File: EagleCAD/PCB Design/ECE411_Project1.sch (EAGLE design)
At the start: 25 parts, among them J1 0473460001_USBMICRO, SW1 FSM2JSMLTR, U1 ATS160SM-1, U2 MIC29310-5.0WU, U3 NCP5501DT50RKG

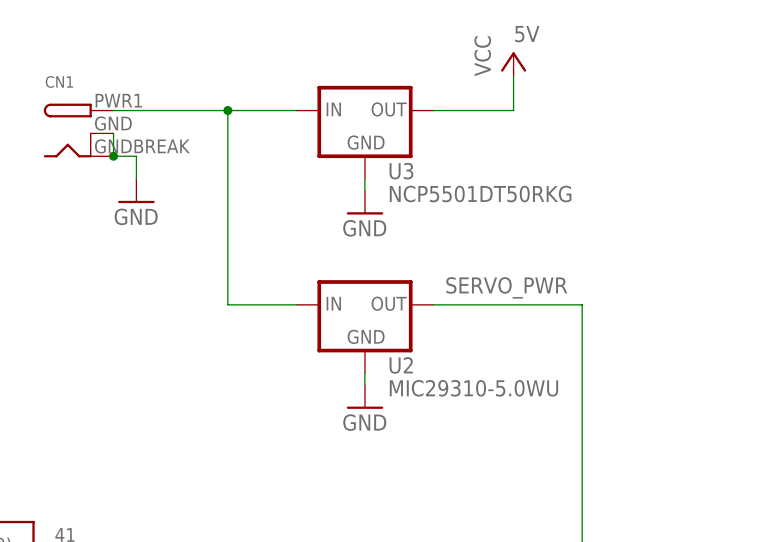
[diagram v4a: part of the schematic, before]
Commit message: Visually complete schematic - nets need to be named still, and erc needs to be run.
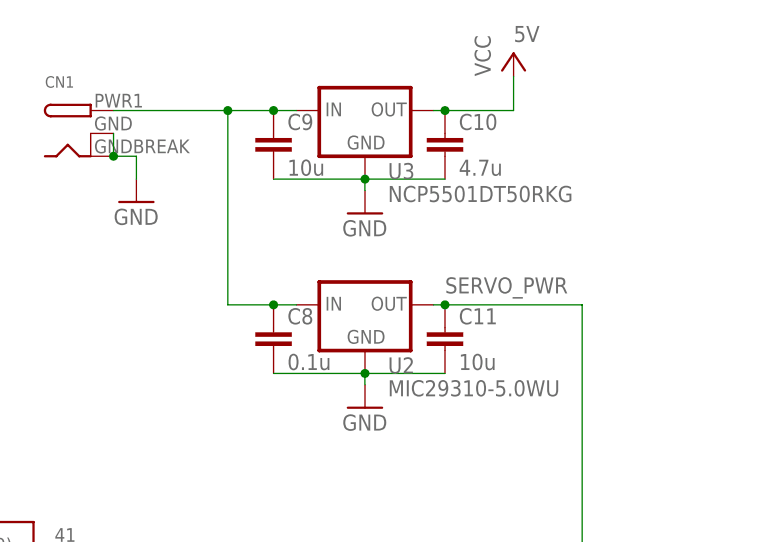
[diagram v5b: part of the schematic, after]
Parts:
- added C10: 4.7u, rcl:C-EUC1206
- added C11, C9: 10u, rcl:C-EUC1206
- added C8: 0.1u, rcl:C-EUC1206
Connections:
- net GND: now also C10.2, C11.2, C8.2, C9.2
- net N$22: now also C8.1, C9.1
- net SERVO_PWR: now also C11.1
- net VCC: now also C10.1
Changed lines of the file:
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@@
 </part>
 <part name="GND15" library="supply1" library_urn="urn:adsk.eagle:library:371" deviceset="GND" device=""/>
+<part name="C8" library="rcl" library_urn="urn:adsk.eagle:library:334" deviceset="C-EU" device="C1206" package3d_urn="urn:adsk.eagle:package:23618/2" value="0.1u"/>
+<part name="C9" library="rcl" library_urn="urn:adsk.eagle:library:334" deviceset="C-EU" device="C1206" package3d_urn="urn:adsk.eagle:package:23618/2" value="10u"/>
+<part name="C10" library="rcl" library_urn="urn:adsk.eagle:library:334" deviceset="C-EU" device="C1206" package3d_urn="urn:adsk.eagle:package:23618/2" value="4.7u"/>
+<part name="C11" library="rcl" library_urn="urn:adsk.eagle:library:334" deviceset="C-EU" device="C1206" package3d_urn="urn:adsk.eagle:package:23618/2" value="10u"/>
 </parts>
 <sheets>
@@
 </instance>
 <instance part="GND15" gate="1" x="33.02" y="121.92"/>
+<instance part="C8" gate="G$1" x="48.26" y="107.95"/>
+<instance part="C9" gate="G$1" x="48.26" y="129.54"/>
+<instance part="C10" gate="G$1" x="67.31" y="129.54"/>
+<instance part="C11" gate="G$1" x="67.31" y="107.95"/>
 </instances>
 <busses>
@@
 <wire x1="58.42" y1="102.87" x2="58.42" y2="101.6" width="0.1524" layer="91"/>
 <pinref part="GND9" gate="1" pin="GND"/>
+<pinref part="C8" gate="G$1" pin="2"/>
+<wire x1="48.26" y1="102.87" x2="58.42" y2="102.87" width="0.1524" layer="91"/>
+<junction x="58.42" y="102.87"/>
+<pinref part="C11" gate="G$1" pin="2"/>
+<wire x1="58.42" y1="102.87" x2="67.31" y2="102.87" width="0.1524" layer="91"/>
 </segment>
 <segment>
@@
 <wire x1="58.42" y1="124.46" x2="58.42" y2="123.19" width="0.1524" layer="91"/>
 <pinref part="GND10" gate="1" pin="GND"/>
+<pinref part="C9" gate="G$1" pin="2"/>
+<wire x1="48.26" y1="124.46" x2="58.42" y2="124.46" width="0.1524" layer="91"/>
+<junction x="58.42" y="124.46"/>
+<pinref part="C10" gate="G$1" pin="2"/>
+<wire x1="58.42" y1="124.46" x2="67.31" y2="124.46" width="0.1524" layer="91"/>
 </segment>
 <segment>
@@
 <segment>
 <pinref part="U3" gate="G$1" pin="OUT"/>
-<wire x1="66.04" y1="132.08" x2="74.93" y2="132.08" width="0.1524" layer="91"/>
+<wire x1="66.04" y1="132.08" x2="67.31" y2="132.08" width="0.1524" layer="91"/>
+<wire x1="67.31" y1="132.08" x2="74.93" y2="132.08" width="0.1524" layer="91"/>
 <wire x1="74.93" y1="132.08" x2="74.93" y2="135.89" width="0.1524" layer="91"/>
 <pinref part="P+4" gate="VCC" pin="VCC"/>
+<pinref part="C10" gate="G$1" pin="1"/>
+<junction x="67.31" y="132.08"/>
 </segment>
 </net>
@@
 <junction x="71.12" y="58.42"/>
 <pinref part="U2" gate="G$1" pin="OUT"/>
-<wire x1="82.55" y1="110.49" x2="66.04" y2="110.49" width="0.1524" layer="91"/>
+<wire x1="82.55" y1="110.49" x2="67.31" y2="110.49" width="0.1524" layer="91"/>
 <label x="67.31" y="111.76" size="1.778" layer="95"/>
+<pinref part="C11" gate="G$1" pin="1"/>
+<wire x1="67.31" y1="110.49" x2="66.04" y2="110.49" width="0.1524" layer="91"/>
+<junction x="67.31" y="110.49"/>
 </segment>
 </net>
@@
 <wire x1="30.48" y1="132.08" x2="43.18" y2="132.08" width="0.1524" layer="91"/>
 <pinref part="U2" gate="G$1" pin="IN"/>
-<wire x1="43.18" y1="132.08" x2="50.8" y2="132.08" width="0.1524" layer="91"/>
-<wire x1="50.8" y1="110.49" x2="43.18" y2="110.49" width="0.1524" layer="91"/>
+<wire x1="43.18" y1="132.08" x2="48.26" y2="132.08" width="0.1524" layer="91"/>
+<wire x1="48.26" y1="132.08" x2="50.8" y2="132.08" width="0.1524" layer="91"/>
+<wire x1="50.8" y1="110.49" x2="48.26" y2="110.49" width="0.1524" layer="91"/>
+<wire x1="48.26" y1="110.49" x2="43.18" y2="110.49" width="0.1524" layer="91"/>
 <wire x1="43.18" y1="110.49" x2="43.18" y2="132.08" width="0.1524" layer="91"/>
 <junction x="43.18" y="132.08"/>
-</segment>
-</net>
+<pinref part="C8" gate="G$1" pin="1"/>
+<junction x="48.26" y="110.49"/>
+<pinref part="C9" gate="G$1" pin="1"/>
+<junction x="48.26" y="132.08"/>
+</segment>
+</net>

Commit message: changed xtal caps to 0805 size from 1206
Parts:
- C6, C7: device rcl:C-EUC1206 -> rcl:C-EUC0805
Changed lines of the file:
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@@
 <part name="LED2" library="led" library_urn="urn:adsk.eagle:library:259" deviceset="LED" device="SMT1206" package3d_urn="urn:adsk.eagle:package:15796/1"/>
 <part name="LED1" library="led" library_urn="urn:adsk.eagle:library:259" deviceset="LED" device="SMT1206" package3d_urn="urn:adsk.eagle:package:15796/1"/>
-<part name="C6" library="rcl" library_urn="urn:adsk.eagle:library:334" deviceset="C-EU" device="C1206" package3d_urn="urn:adsk.eagle:package:23618/2" value="22p"/>
-<part name="C7" library="rcl" library_urn="urn:adsk.eagle:library:334" deviceset="C-EU" device="C1206" package3d_urn="urn:adsk.eagle:package:23618/2" value="22p"/>
 <part name="GND14" library="supply1" library_urn="urn:adsk.eagle:library:371" deviceset="GND" device=""/>
 <part name="P+2" library="supply1" library_urn="urn:adsk.eagle:library:371" deviceset="VCC" device="">
@@
 <part name="C10" library="rcl" library_urn="urn:adsk.eagle:library:334" deviceset="C-EU" device="C1206" package3d_urn="urn:adsk.eagle:package:23618/2" value="4.7u"/>
 <part name="C11" library="rcl" library_urn="urn:adsk.eagle:library:334" deviceset="C-EU" device="C1206" package3d_urn="urn:adsk.eagle:package:23618/2" value="10u"/>
+<part name="C6" library="rcl" library_urn="urn:adsk.eagle:library:334" deviceset="C-EU" device="C0805" package3d_urn="urn:adsk.eagle:package:23617/2" value="22p"/>
+<part name="C7" library="rcl" library_urn="urn:adsk.eagle:library:334" deviceset="C-EU" device="C0805" package3d_urn="urn:adsk.eagle:package:23617/2" value="22p"/>
 </parts>
 <sheets>
@@
 <instance part="LED2" gate="G$1" x="30.48" y="-10.16"/>
 <instance part="LED1" gate="G$1" x="39.37" y="-10.16"/>
-<instance part="C6" gate="G$1" x="-35.56" y="39.37" rot="R90"/>
-<instance part="C7" gate="G$1" x="-35.56" y="29.21" rot="R90"/>
 <instance part="GND14" gate="1" x="-38.1" y="24.13"/>
 <instance part="P+2" gate="VCC" x="-26.67" y="74.93">
@@
 <instance part="C10" gate="G$1" x="67.31" y="129.54"/>
 <instance part="C11" gate="G$1" x="67.31" y="107.95"/>
+<instance part="C6" gate="G$1" x="-35.56" y="39.37" rot="R90"/>
+<instance part="C7" gate="G$1" x="-35.56" y="29.21" rot="R90"/>
 </instances>
 <busses>
@@
 </segment>
 <segment>
+<wire x1="-38.1" y1="39.37" x2="-38.1" y2="29.21" width="0.1524" layer="91"/>
+<wire x1="-38.1" y1="29.21" x2="-38.1" y2="26.67" width="0.1524" layer="91"/>
+<pinref part="GND14" gate="1" pin="GND"/>
 <pinref part="C6" gate="G$1" pin="1"/>
 <pinref part="C7" gate="G$1" pin="1"/>
-<wire x1="-38.1" y1="39.37" x2="-38.1" y2="29.21" width="0.1524" layer="91"/>
-<wire x1="-38.1" y1="29.21" x2="-38.1" y2="26.67" width="0.1524" layer="91"/>
 <junction x="-38.1" y="29.21"/>
-<pinref part="GND14" gate="1" pin="GND"/>
 </segment>
 <segment>
@@
 <segment>
 <wire x1="-29.21" y1="29.21" x2="-26.67" y2="29.21" width="0.1524" layer="91"/>
-<pinref part="C7" gate="G$1" pin="2"/>
 <wire x1="-26.67" y1="29.21" x2="-24.13" y2="29.21" width="0.1524" layer="91"/>
 <wire x1="-29.21" y1="29.21" x2="-30.48" y2="29.21" width="0.1524" layer="91"/>
@@
 <pinref part="U1" gate="G$1" pin="1"/>
 <junction x="-26.67" y="29.21"/>
+<pinref part="C7" gate="G$1" pin="2"/>
 </segment>
 </net>
@@
 <segment>
 <wire x1="-24.13" y1="39.37" x2="-26.67" y2="39.37" width="0.1524" layer="91"/>
-<pinref part="C6" gate="G$1" pin="2"/>
 <wire x1="-26.67" y1="39.37" x2="-29.21" y2="39.37" width="0.1524" layer="91"/>
 <wire x1="-29.21" y1="39.37" x2="-30.48" y2="39.37" width="0.1524" layer="91"/>
@@
 <pinref part="U1" gate="G$1" pin="2"/>
 <junction x="-26.67" y="39.37"/>
-</segment>
-</net>
+<pinref part="C6" gate="G$1" pin="2"/>
+</segment>
+</net>

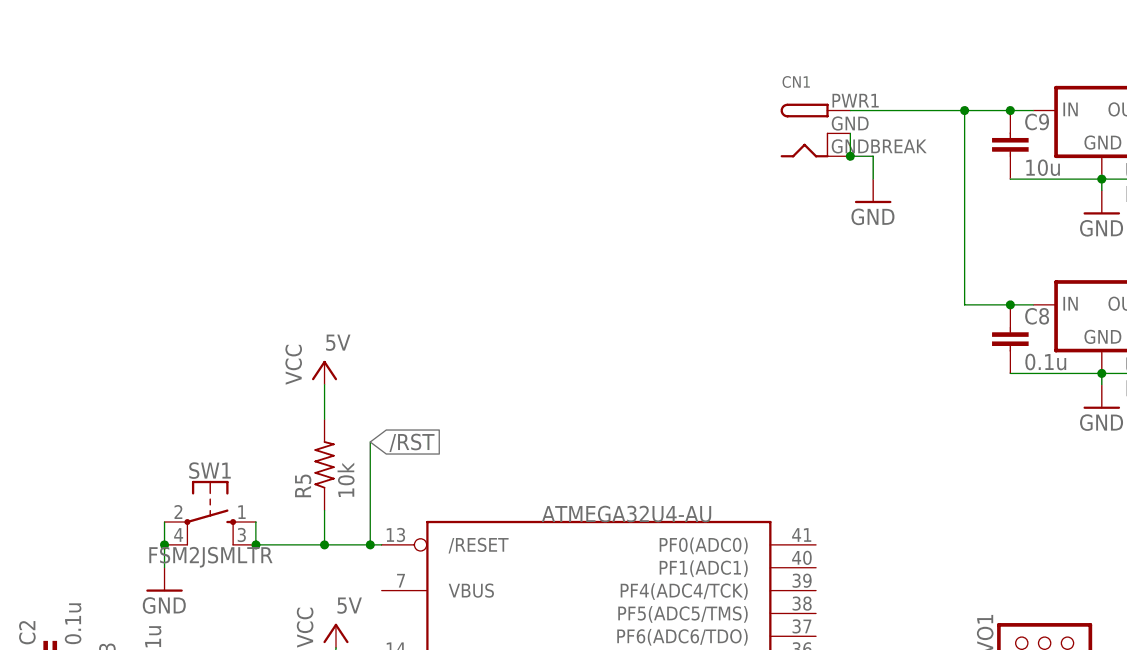
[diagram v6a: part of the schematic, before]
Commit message: Updated schematic with new DC barrel component that is thru-hole 2.1MM size
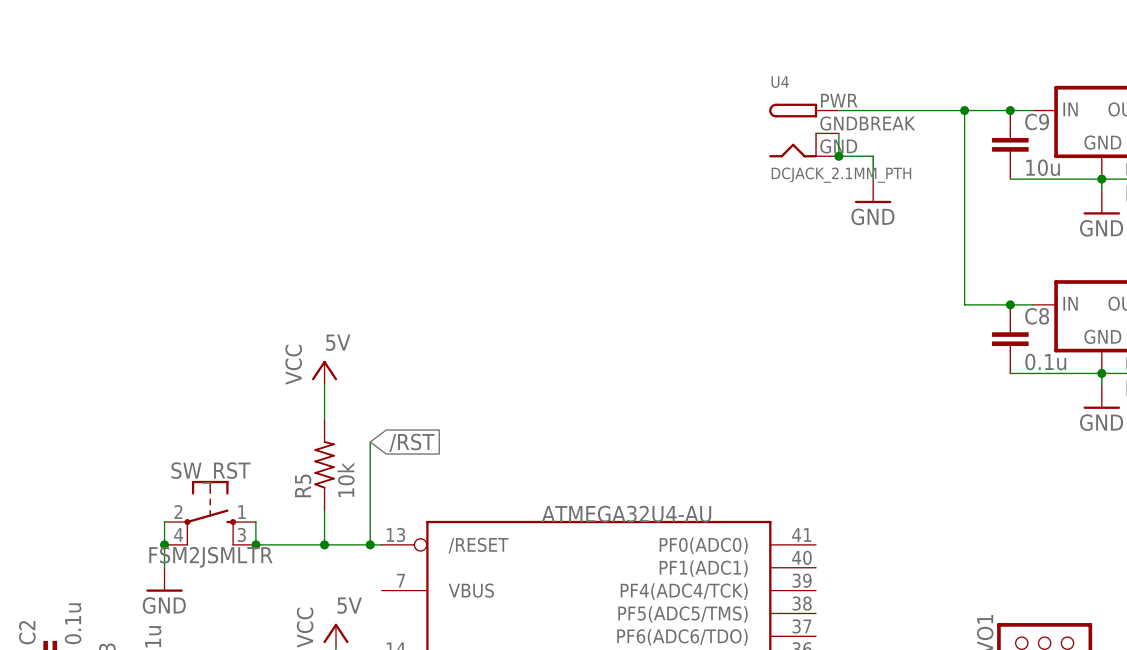
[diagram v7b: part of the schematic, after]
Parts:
- removed CN1: (no value), adafruit:DCBARRELSMT
- added U4: DCJACK_2.1MM_PTH, DCBARREL_2.1MM:DCJACK_2.1MM_PTH
- renumbered SW1 to SW_RST
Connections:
- net N$1 renamed D+USB
- net N$2 renamed D+MCU
- net N$3 renamed D-USB
- net N$4 renamed D-MCU
- net GND: now also U4.GND, U4.GNDBREAK; no longer CN1.GND, CN1.GNDBREAK
- net N$22: now also U4.PWR; no longer CN1.PWR
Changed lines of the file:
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@@
 <attribute name="VCC" value="5V"/>
 </part>
-<part name="SW1" library="Push_Button" deviceset="FSM2JSMLTR" device=""/>
+<part name="SW_RST" library="Push_Button" deviceset="FSM2JSMLTR" device=""/>
 <part name="J1" library="USB_Micro_and_AVRISP" deviceset="0473460001_USBMICRO" device=""/>
 <part name="ISP1" library="USB_Micro_and_AVRISP" deviceset="AVRISP" device="-6"/>
 <part name="U1" library="Xtals" deviceset="ATS160SM-1" device=""/>
-<part name="CN1" library="adafruit" library_urn="urn:adsk.eagle:library:420" deviceset="DCBARREL" device="SMT" package3d_urn="urn:adsk.eagle:package:6240730/1"/>
 <part name="U2" library="Regulators" deviceset="MIC29310-5.0WU" device=""/>
 <part name="U3" library="Regulators" deviceset="NCP5501DT50RKG" device=""/>
@@
 <part name="C6" library="rcl" library_urn="urn:adsk.eagle:library:334" deviceset="C-EU" device="C0805" package3d_urn="urn:adsk.eagle:package:23617/2" value="22p"/>
 <part name="C7" library="rcl" library_urn="urn:adsk.eagle:library:334" deviceset="C-EU" device="C0805" package3d_urn="urn:adsk.eagle:package:23617/2" value="22p"/>
+<part name="U4" library="DCBARREL_2.1MM" deviceset="DCJACK_2.1MM_PTH" device=""/>
 </parts>
 <sheets>
@@
 <attribute name="VCC" x="-26.67" y="76.2" size="1.778" layer="96"/>
 </instance>
-<instance part="SW1" gate="G$1" x="-40.64" y="86.36"/>
+<instance part="SW_RST" gate="G$1" x="-40.64" y="86.36"/>
 <instance part="J1" gate="G$1" x="-96.52" y="50.8"/>
 <instance part="ISP1" gate="G$1" x="78.74" y="26.67"/>
 <instance part="U1" gate="G$1" x="-26.67" y="34.29" rot="R90"/>
-<instance part="CN1" gate="G$1" x="27.94" y="129.54"/>
 <instance part="U2" gate="G$1" x="58.42" y="110.49"/>
 <instance part="U3" gate="G$1" x="58.42" y="132.08"/>
@@
 <instance part="C6" gate="G$1" x="-35.56" y="39.37" rot="R90"/>
 <instance part="C7" gate="G$1" x="-35.56" y="29.21" rot="R90"/>
+<instance part="U4" gate="G$1" x="26.67" y="129.54"/>
 </instances>
 <busses>
@@
 <pinref part="GND7" gate="1" pin="GND"/>
 <wire x1="-45.72" y1="81.28" x2="-45.72" y2="83.82" width="0.1524" layer="91"/>
-<pinref part="SW1" gate="G$1" pin="4"/>
-<pinref part="SW1" gate="G$1" pin="2"/>
+<pinref part="SW_RST" gate="G$1" pin="4"/>
+<pinref part="SW_RST" gate="G$1" pin="2"/>
 <wire x1="-45.72" y1="83.82" x2="-45.72" y2="86.36" width="0.1524" layer="91"/>
 <junction x="-45.72" y="83.82"/>
@@
 </segment>
 <segment>
-<pinref part="CN1" gate="G$1" pin="GNDBREAK"/>
-<pinref part="CN1" gate="G$1" pin="GND"/>
-<wire x1="30.48" y1="129.54" x2="30.48" y2="127" width="0.1524" layer="91"/>
-<wire x1="30.48" y1="127" x2="33.02" y2="127" width="0.1524" layer="91"/>
+<wire x1="29.21" y1="129.54" x2="29.21" y2="127" width="0.1524" layer="91"/>
+<wire x1="29.21" y1="127" x2="33.02" y2="127" width="0.1524" layer="91"/>
 <wire x1="33.02" y1="127" x2="33.02" y2="124.46" width="0.1524" layer="91"/>
-<junction x="30.48" y="127"/>
 <pinref part="GND15" gate="1" pin="GND"/>
-</segment>
-</net>
-<net name="N$1" class="0">
+<pinref part="U4" gate="G$1" pin="GNDBREAK"/>
+<pinref part="U4" gate="G$1" pin="GND"/>
+<junction x="29.21" y="127"/>
+</segment>
+</net>
+<net name="D+USB" class="0">
 <segment>
 <wire x1="-77.47" y1="53.34" x2="-86.36" y2="53.34" width="0.1524" layer="91"/>
@@
 </segment>
 </net>
-<net name="N$2" class="0">
+<net name="D+MCU" class="0">
 <segment>
 <pinref part="U$1" gate="G$1" pin="D+"/>
@@
 </segment>
 </net>
-<net name="N$3" class="0">
+<net name="D-USB" class="0">
 <segment>
 <wire x1="-86.36" y1="50.8" x2="-64.77" y2="50.8" width="0.1524" layer="91"/>
@@
 </segment>
 </net>
-<net name="N$4" class="0">
+<net name="D-MCU" class="0">
 <segment>
 <wire x1="-54.61" y1="50.8" x2="-29.21" y2="50.8" width="0.1524" layer="91"/>
@@
 <junction x="-27.94" y="83.82"/>
 <pinref part="R5" gate="G$1" pin="1"/>
-<pinref part="SW1" gate="G$1" pin="3"/>
-<pinref part="SW1" gate="G$1" pin="1"/>
+<pinref part="SW_RST" gate="G$1" pin="3"/>
+<pinref part="SW_RST" gate="G$1" pin="1"/>
 <wire x1="-35.56" y1="83.82" x2="-35.56" y2="86.36" width="0.1524" layer="91"/>
 <junction x="-35.56" y="83.82"/>
@@
 <net name="N$22" class="0">
 <segment>
-<pinref part="CN1" gate="G$1" pin="PWR"/>
 <pinref part="U3" gate="G$1" pin="IN"/>
-<wire x1="30.48" y1="132.08" x2="43.18" y2="132.08" width="0.1524" layer="91"/>
+<wire x1="29.21" y1="132.08" x2="43.18" y2="132.08" width="0.1524" layer="91"/>
 <pinref part="U2" gate="G$1" pin="IN"/>
 <wire x1="43.18" y1="132.08" x2="48.26" y2="132.08" width="0.1524" layer="91"/>
@@
 <pinref part="C9" gate="G$1" pin="1"/>
 <junction x="48.26" y="132.08"/>
-</segment>
-</net>
+<pinref part="U4" gate="G$1" pin="PWR"/>
+</segment>
+</net>

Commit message: Started the PCB - Everything's on the board and messy!
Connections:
- net N$20 renamed XTAL2
- net N$21 renamed XTAL1
- net N$22 renamed UNREG_PWR
- net N$5 renamed UCAP
- removed net N$15: ISP1.VCC
- net GND: no longer U4.GNDBREAK
- net VCC: now also ISP1.VCC
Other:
- moved on the sheet: C10, C11, C8, C9, U2, U3, U4
